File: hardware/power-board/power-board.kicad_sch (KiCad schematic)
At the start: 30 parts, among them J1 SW_SPST, J2 Main Board, J3 DMX512 Out Jack, J4 DMX512, K1 SPST-NO, K2 SPST-NO, P1 IEC320-C14, P2 IEC320-C13, P3 IEC320-C13, U1 SZNUD3124DMT1G, U2 THVD1439

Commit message: Change power board mounting hole footprints
This changes them from the 3.2mm diameter M3 version to the
similar-looking 3.5mm diameter version. Position is still the same, and
the size isn't that different, but this should provide more flexibility
when rear panel alignment tolerances cause issue with the internal screw
holes lining up.

Fix #53
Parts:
- H1, H2: footprint MountingHole:MountingHole_3.2mm_M3_Pad_Via -> MountingHole:MountingHole_3.5mm_Pad_Via
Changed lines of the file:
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@@
 			)
 		)
-		(property "Footprint" "MountingHole:MountingHole_3.2mm_M3_Pad_Via"
+		(property "Footprint" "MountingHole:MountingHole_3.5mm_Pad_Via"
 			(at 91.44 99.06 0)
 			(effects
@@
 			)
 		)
-		(property "Footprint" "MountingHole:MountingHole_3.2mm_M3_Pad_Via"
+		(property "Footprint" "MountingHole:MountingHole_3.5mm_Pad_Via"
 			(at 91.44 104.14 0)
 			(effects

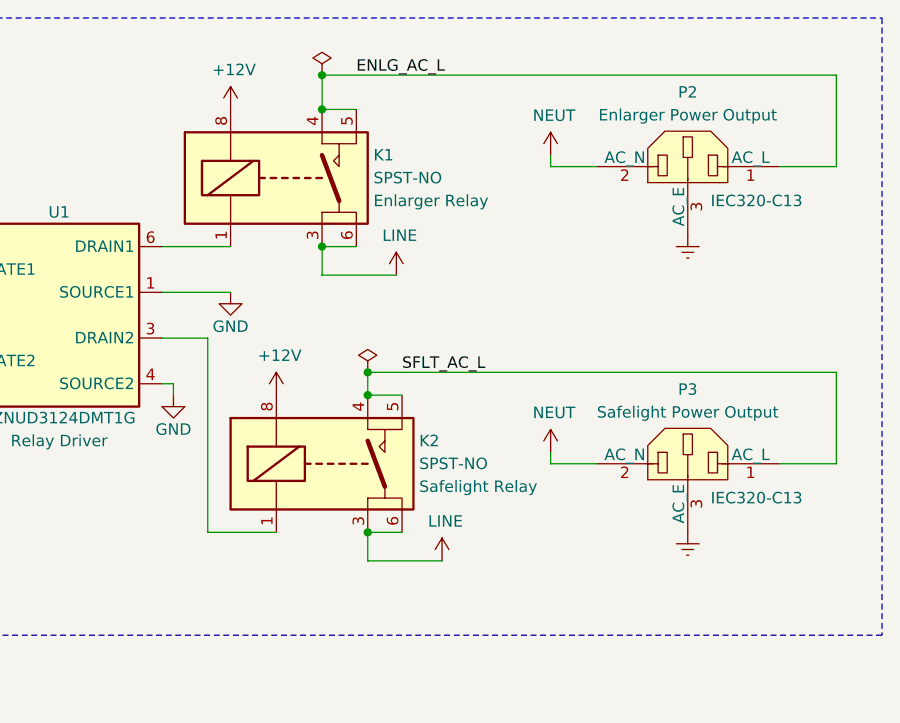
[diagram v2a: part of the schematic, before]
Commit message: Revert relays from G2RL-1A-E to G2RL-1A
We really don't need 16A rated relays here, as 12A is already way over
what we're fusing at or plan to support in the power switch connection.

Also decided this time to go with the flux protected 1A model rather
than the fully sealed 1A4 model, because the venting likely helps with
relay life and the relay won't need post-processing steps. Just need to
make sure the board isn't immersed after soldering, but that may related
to other components as well.
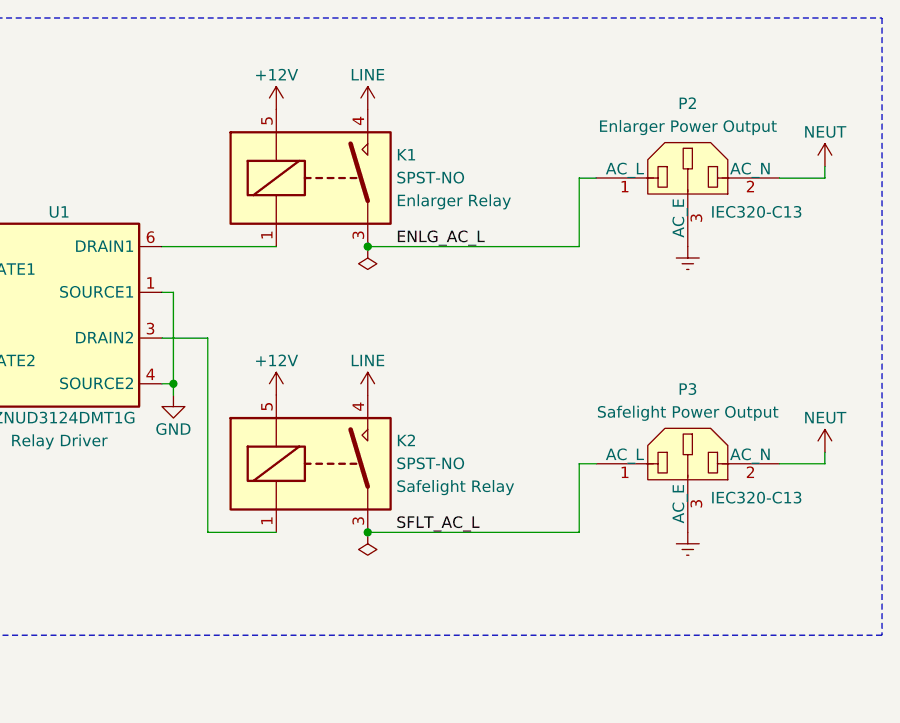
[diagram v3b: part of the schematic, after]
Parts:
- K1, K2: footprint lib_fp:Relay_SPST_Omron_G2RL-1A-E -> lib_fp:Relay_SPST_Omron_G2RL-1A; symbol Project:G2RL-1A4-E-DC12 -> Project:G2RL-1A4-DC12; Manufacturer PN G2RL-1A4-E DC12 -> G2RL-1A DC12; Supplier PN Z3083-ND -> Z140-ND
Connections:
- net +12V: now also K1.5, K2.5; no longer K1.8, K2.8
- net ENLG_AC_L: now also K1.3; no longer K1.4, K1.5
- net LINE: now also K1.4, K2.4; no longer K1.3, K1.6, K2.3, K2.6
- net SFLT_AC_L: now also K2.3; no longer K2.4, K2.5
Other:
- moved on the sheet: P2

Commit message: Change power switch connector from Mega-Fit to Mini-Fit Jr
This swaps the power connector for a smaller one, and moves it slightly
to resolve mechanical clearance issues. Fixes #52

Some routing cleanup may still be needed, but it'll be done as part of
future changes.
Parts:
- J1: footprint Connector_Molex:Molex_Mega-Fit_76829-0002_2x01_P5.70mm_Vertical -> lib_fp:Molex_Mini-Fit_Jr_172447_2x01_P4.20mm_Vertical; Manufacturer PN 0768290002 -> 1724470002; Supplier Digi-Key -> Mouser; Supplier PN WM11975-ND -> 538-172447-0002
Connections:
- net LINE: now also J1.2 (B); no longer J1.1 (A)
- net at F1.1: now also J1.1 (A); no longer J1.2 (B)
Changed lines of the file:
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@@
 		(lib_id "Switch:SW_SPST")
 		(at 41.91 52.07 0)
-		(mirror y)
 		(unit 1)
 		(exclude_from_sim no)
@@
 			)
 		)
-		(property "Footprint" "Connector_Molex:Molex_Mega-Fit_76829-0002_2x01_P5.70mm_Vertical"
+		(property "Footprint" "lib_fp:Molex_Mini-Fit_Jr_172447_2x01_P4.20mm_Vertical"
 			(at 41.91 52.07 0)
 			(effects
@@
 			)
 		)
-		(property "Datasheet" "https://www.molex.com/en-us/products/part-detail/768290002?display=pdf"
+		(property "Datasheet" "https://www.molex.com/en-us/products/part-detail/1724470002?display=pdf"
 			(at 41.91 52.07 0)
 			(effects
@@
 			)
 		)
-		(property "Manufacturer PN" "0768290002"
+		(property "Manufacturer PN" "1724470002"
 			(at 41.91 52.07 0)
 			(effects
@@
 			)
 		)
-		(property "Supplier" "Digi-Key"
+		(property "Supplier" "Mouser"
 			(at 41.91 52.07 0)
 			(effects
@@
 			)
 		)
-		(property "Supplier PN" "WM11975-ND"
+		(property "Supplier PN" "538-172447-0002"
 			(at 41.91 52.07 0)
 			(effects

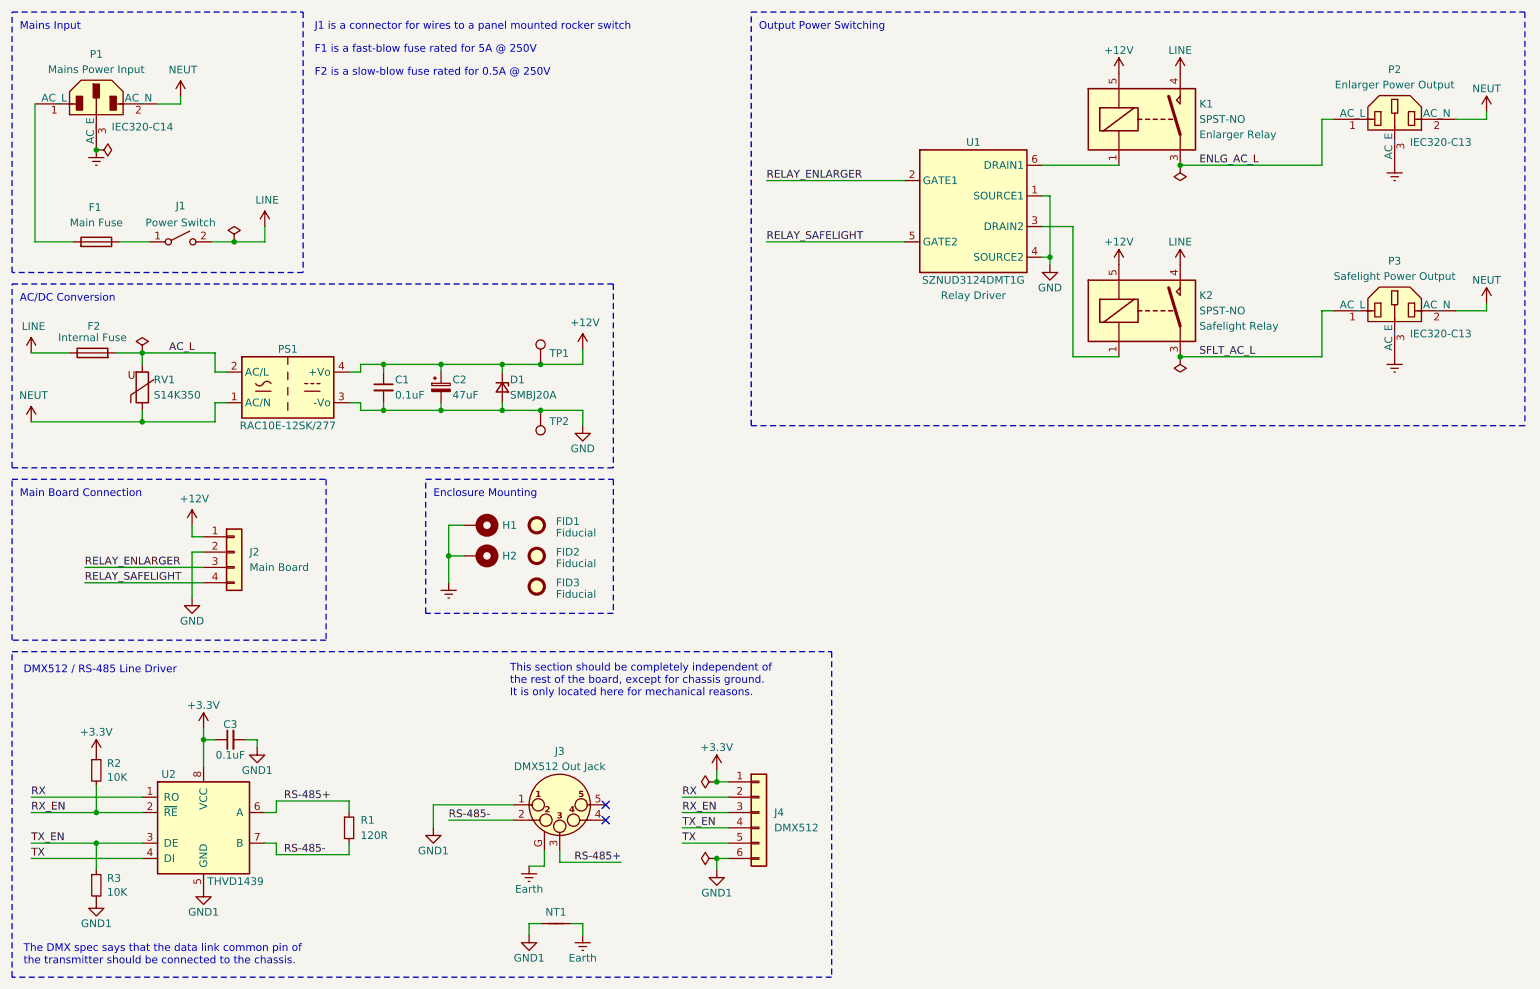
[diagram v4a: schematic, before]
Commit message: Add filtering components to input of AC/DC converter
Remove the internal fuse and MOV, since they appear to be redundant with
components already inside the sealed AC/DC converter block.

Add AC line filter to the input of the AC/DC converter, to help reduce
problems caused by external line noise.

Standardize on slightly thinner power traces and a 2.5mm clearance rule, to
make sure everything fits.  With 2oz copper, this should still be okay.

Refs #56
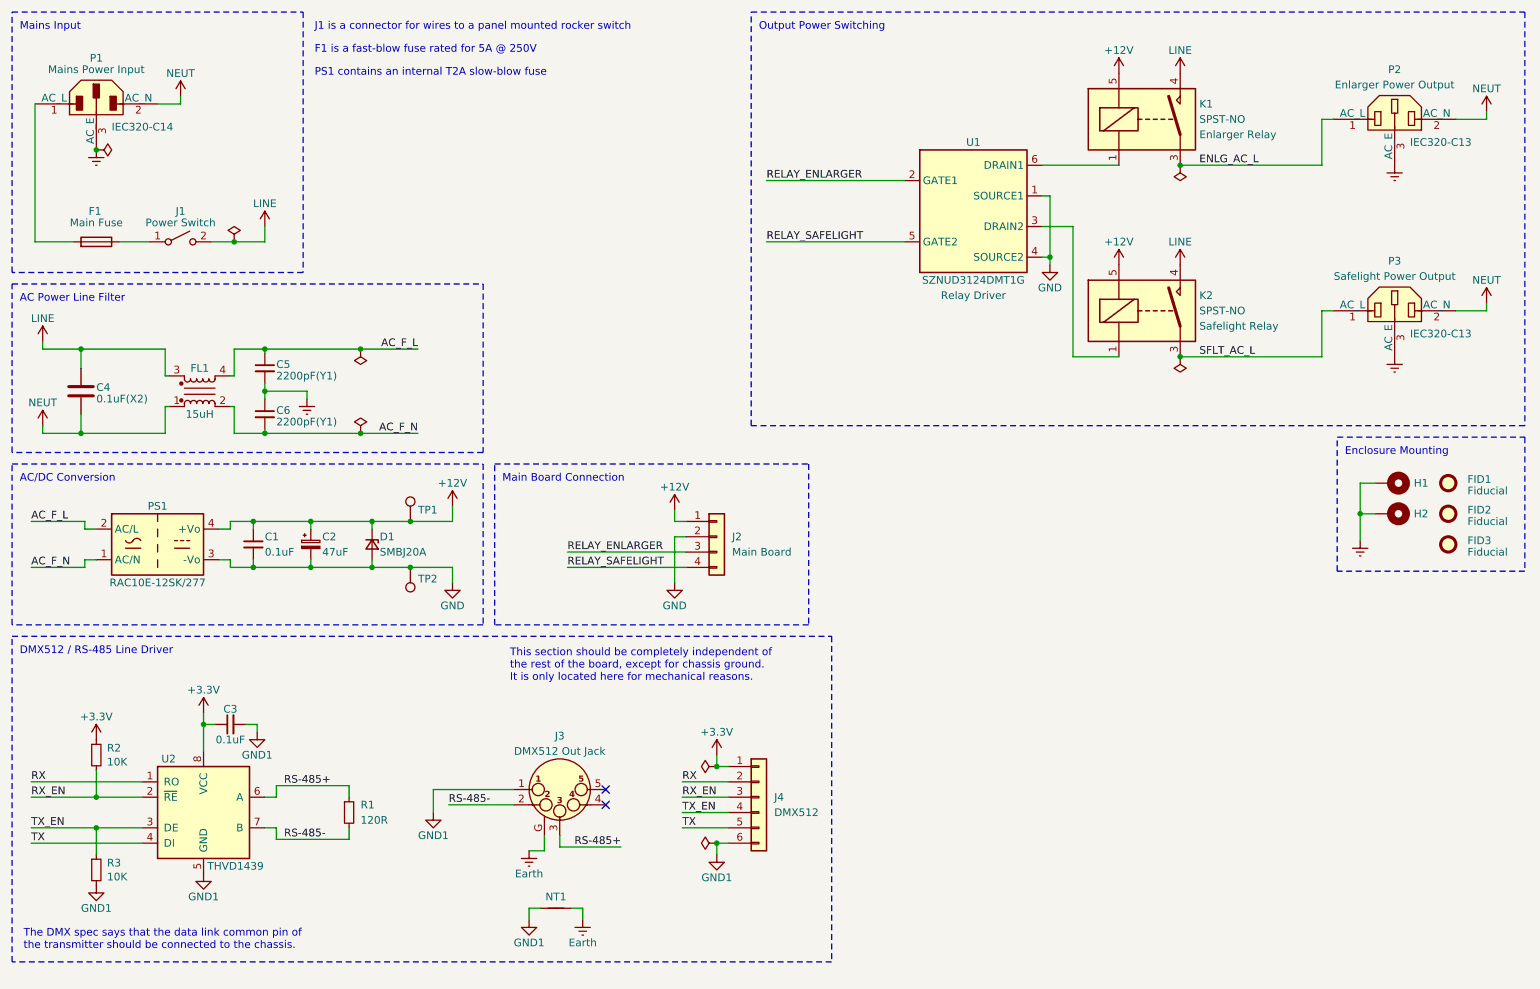
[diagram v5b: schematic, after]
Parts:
- removed F2: Fuse, Fuse:Fuseholder_Cylinder-5x20mm_Schurter_0031_8201_Horizontal_Open, symbol Device:Fuse
- removed RV1: S14K350, lib_fp:RV_Disc_D15.5mm_W5.6mm_P7.5mm, symbol Device:Varistor
- added C4: 0.1uF(X2), lib_fp:C_Rect_L18.0mm_W5.0mm_P15.00mm_Kemet_R46, symbol Device:C
- added C5, C6: 2200pF(Y1), lib_fp:C_Disc_D12.0mm_W5.0mm_P10.00mm_Vishay_VY1, symbol Device:C_Small
- added FL1: 15uH, lib_fp:Choke_Schaffner_RN212-02-12.5x18.0mm, symbol Filter:Choke_Schaffner_RN102-0.3-02-22M
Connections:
- net Earth: now also C5.2, C6.1
- net LINE: now also C4.1, FL1.3
- net NEUT: now also C4.2, FL1.1; no longer PS1.1 (AC/N)
- net AC_L renamed AC_F_L
- net AC_F_L: now also C5.1, FL1.4
- new net AC_F_N: C6.2, FL1.2, PS1.1 (AC/N)
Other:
- note added: "AC Power Line Filter"
- note added: "PS1 contains an internal T2A slow-blow fuse"
- note removed: "F2 is a slow-blow fuse rated for 0.5A @ 250V"
- moved on the sheet: C1, C2, C3, D1, FID1, FID2, FID3, H1, H2, J2, J3, J4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

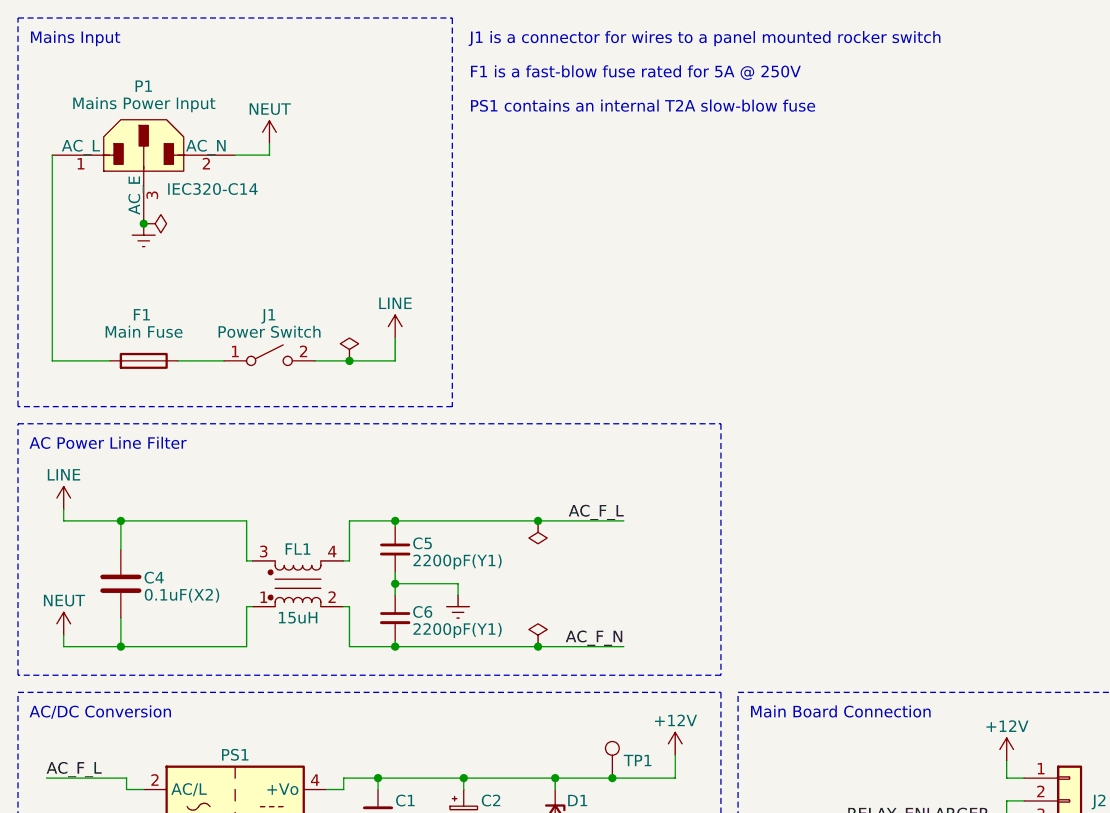
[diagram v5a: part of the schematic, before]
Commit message: Numerous updates and tweaks to power board EMI filter addition
Refs #56

Swapped all of the main filter components with slightly smaller
versions, to help with clearance for main power traces.
Added a UL1676 recognized resistor to act as a bleeder for the X
capacitor.

Arranged traces to keep at least 3mm clearance between all mains AC
traces, and >4mm clearance between any mains AC trace and the DC side.
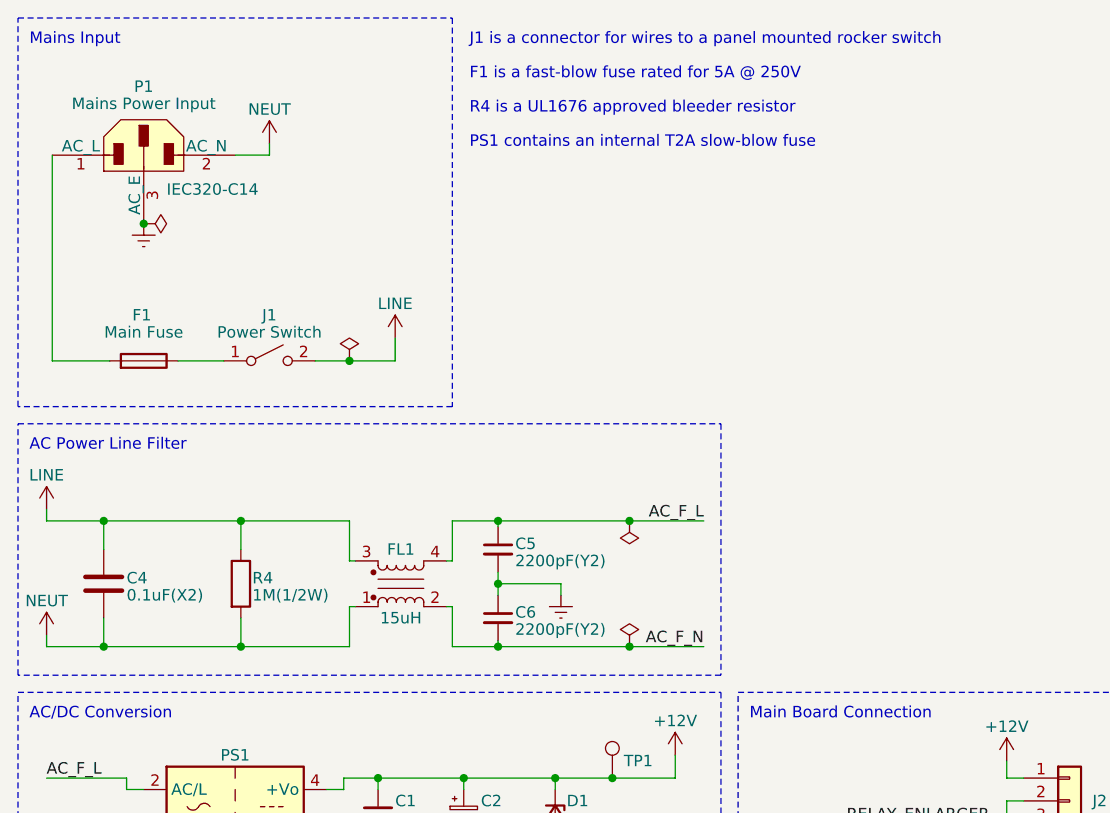
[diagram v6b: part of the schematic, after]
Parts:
- added R4: 1M(1/2W), Resistor_THT:R_Axial_DIN0309_L9.0mm_D3.2mm_P12.70mm_Horizontal, symbol Device:R
- C4: footprint lib_fp:C_Rect_L18.0mm_W5.0mm_P15.00mm_Kemet_R46 -> lib_fp:C_Rect_L13.0mm_W5.0mm_P10.00mm_Kemet_R46; Manufacturer PN R46KI3100JHM1M -> R46KF310000P1M; Supplier PN 399-R46KI3100JHM1M-ND -> 399-9642-ND
- C5, C6: value 2200pF(Y1) -> 2200pF(Y2); footprint lib_fp:C_Disc_D12.0mm_W5.0mm_P10.00mm_Vishay_VY1 -> lib_fp:C_Disc_D8.0mm_W5.0mm_P7.50mm_Vishay_VY2; Manufacturer PN VY1222M47Y5UQ6UV0 -> VY2222M31Y5VS63V7; Supplier PN BC5245CT-ND -> BC3309-ND
- FL1: footprint lib_fp:Choke_Schaffner_RN212-02-12.5x18.0mm -> lib_fp:Choke_Schaffner_RN112-02-17.7x17.1mm; Manufacturer PN RN212-0.6-02-15M -> RN112-0.6-02-15M; Supplier PN 817-2168-ND -> 817-2092-ND
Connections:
- net LINE: now also R4.1
- net NEUT: now also R4.2
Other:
- note added: "R4 is a UL1676 approved bleeder resistor"
- moved on the sheet: C4, C5, C6, FL1
